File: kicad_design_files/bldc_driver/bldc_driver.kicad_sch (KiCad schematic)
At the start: 2 parts

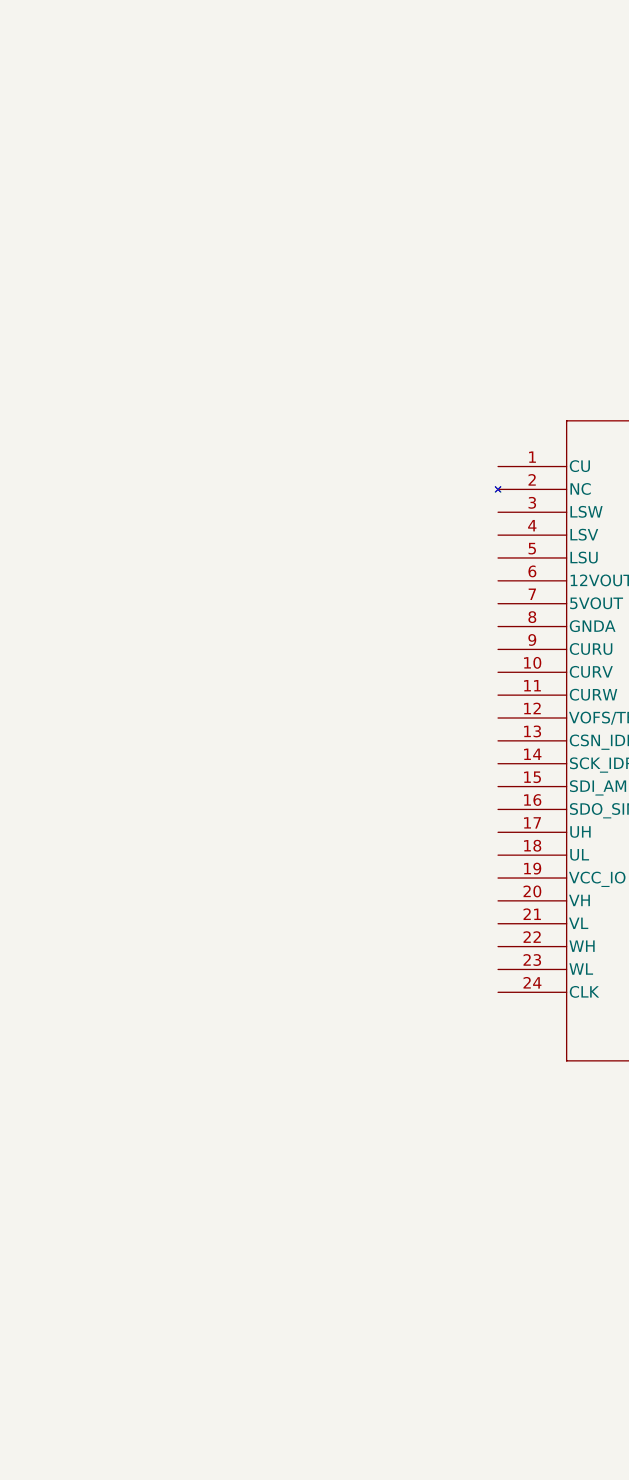
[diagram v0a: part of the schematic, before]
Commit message: MOSFET is determined
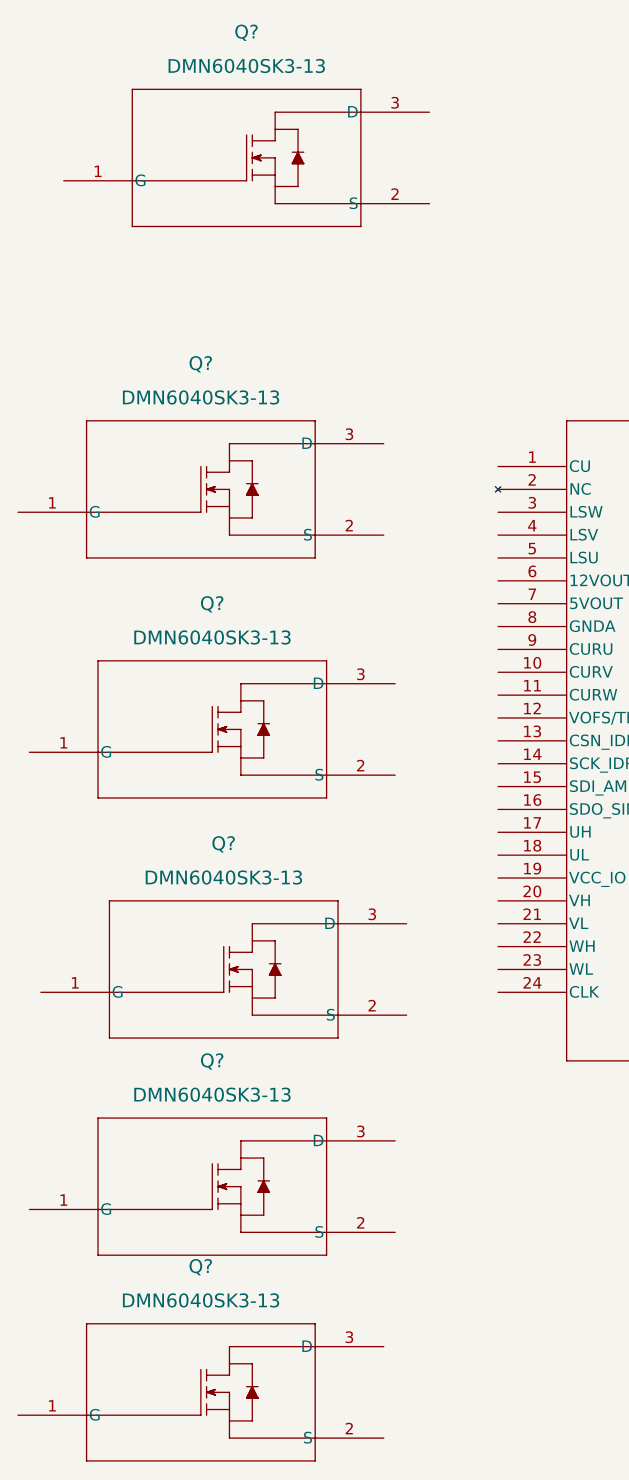
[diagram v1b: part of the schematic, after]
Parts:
- added Q? (x6): DMN6040SK3-13, bldcDriverFootprintLibrary:D-PAK_DMN6040SK3-13_DIO, symbol bldcDriverLibrary:DMN6040SK3-13
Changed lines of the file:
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@@
 (kicad_sch (version 20211123) (generator eeschema)
   (paper "A4")
+  (symbol (lib_id "bldcDriverLibrary:DMN6040SK3-13") (at 26.67 97.79 0) (unit 1)
+    (in_bom yes) (on_board yes) (fields_autoplaced)
+    (property "Reference" "Q?" (id 0) (at 46.99 81.28 0)
+      (effects (font (size 1.524 1.524)))
+    )
+    (property "Value" "DMN6040SK3-13" (id 1) (at 46.99 85.09 0)
+      (effects (font (size 1.524 1.524)))
+    )
+    (property "Footprint" "bldcDriverFootprintLibrary:D-PAK_DMN6040SK3-13_DIO" (id 2) (at 26.67 97.79 0)
+      (effects (font (size 1.27 1.27) italic) hide)
+    )
+    (property "Datasheet" "DMN6040SK3-13" (id 3) (at 26.67 97.79 0)
+      (effects (font (size 1.27 1.27) italic) hide)
+    )
+    (pin "1")
+    (pin "2")
+    (pin "3")
+  )
+  (symbol (lib_id "bldcDriverLibrary:DMN6040SK3-13") (at 27.94 124.46 0) (unit 1)
+    (in_bom yes) (on_board yes) (fields_autoplaced)
+    (property "Reference" "Q?" (id 0) (at 48.26 107.95 0)
+      (effects (font (size 1.524 1.524)))
+    )
+    (property "Value" "DMN6040SK3-13" (id 1) (at 48.26 111.76 0)
+      (effects (font (size 1.524 1.524)))
+    )
+    (property "Footprint" "bldcDriverFootprintLibrary:D-PAK_DMN6040SK3-13_DIO" (id 2) (at 27.94 124.46 0)
+      (effects (font (size 1.27 1.27) italic) hide)
+    )
+    (property "Datasheet" "DMN6040SK3-13" (id 3) (at 27.94 124.46 0)
+      (effects (font (size 1.27 1.27) italic) hide)
+    )
+    (pin "1")
+    (pin "2")
+    (pin "3")
+  )
   (symbol (lib_id "bldcDriverLibrary:TMC6200-TA-T") (at 78.74 66.04 0) (unit 1)
     (in_bom yes) (on_board yes) (fields_autoplaced)
@@
     (pin "EPAD")
   )
+  (symbol (lib_id "bldcDriverLibrary:DMN6040SK3-13") (at 25.4 71.12 0) (unit 1)
+    (in_bom yes) (on_board yes) (fields_autoplaced)
+    (property "Reference" "Q?" (id 0) (at 45.72 54.61 0)
+      (effects (font (size 1.524 1.524)))
+    )
+    (property "Value" "DMN6040SK3-13" (id 1) (at 45.72 58.42 0)
+      (effects (font (size 1.524 1.524)))
+    )
+    (property "Footprint" "bldcDriverFootprintLibrary:D-PAK_DMN6040SK3-13_DIO" (id 2) (at 25.4 71.12 0)
+      (effects (font (size 1.27 1.27) italic) hide)
+    )
+    (property "Datasheet" "DMN6040SK3-13" (id 3) (at 25.4 71.12 0)
+      (effects (font (size 1.27 1.27) italic) hide)
+    )
+    (pin "1")
+    (pin "2")
+    (pin "3")
+  )
   (symbol (lib_id "bldcDriverLibrary:ESP32-WROOM-32U") (at 234.95 91.44 0) (unit 1)
     (in_bom yes) (on_board yes) (fields_autoplaced)
@@
     (pin "9")
   )
+  (symbol (lib_id "bldcDriverLibrary:DMN6040SK3-13") (at 30.48 34.29 0) (unit 1)
+    (in_bom yes) (on_board yes) (fields_autoplaced)
+    (property "Reference" "Q?" (id 0) (at 50.8 17.78 0)
+      (effects (font (size 1.524 1.524)))
+    )
+    (property "Value" "DMN6040SK3-13" (id 1) (at 50.8 21.59 0)
+      (effects (font (size 1.524 1.524)))
+    )
+    (property "Footprint" "bldcDriverFootprintLibrary:D-PAK_DMN6040SK3-13_DIO" (id 2) (at 30.48 34.29 0)
+      (effects (font (size 1.27 1.27) italic) hide)
+    )
+    (property "Datasheet" "DMN6040SK3-13" (id 3) (at 30.48 34.29 0)
+      (effects (font (size 1.27 1.27) italic) hide)
+    )
+    (pin "1")
+    (pin "2")
+    (pin "3")
+  )
+  (symbol (lib_id "bldcDriverLibrary:DMN6040SK3-13") (at 25.4 171.45 0) (unit 1)
+    (in_bom yes) (on_board yes) (fields_autoplaced)
+    (property "Reference" "Q?" (id 0) (at 45.72 154.94 0)
+      (effects (font (size 1.524 1.524)))
+    )
+    (property "Value" "DMN6040SK3-13" (id 1) (at 45.72 158.75 0)
+      (effects (font (size 1.524 1.524)))
+    )
+    (property "Footprint" "bldcDriverFootprintLibrary:D-PAK_DMN6040SK3-13_DIO" (id 2) (at 25.4 171.45 0)
+      (effects (font (size 1.27 1.27) italic) hide)
+    )
+    (property "Datasheet" "DMN6040SK3-13" (id 3) (at 25.4 171.45 0)
+      (effects (font (size 1.27 1.27) italic) hide)
+    )
+    (pin "1")
+    (pin "2")
+    (pin "3")
+  )
+  (symbol (lib_id "bldcDriverLibrary:DMN6040SK3-13") (at 26.67 148.59 0) (unit 1)
+    (in_bom yes) (on_board yes) (fields_autoplaced)
+    (property "Reference" "Q?" (id 0) (at 46.99 132.08 0)
+      (effects (font (size 1.524 1.524)))
+    )
+    (property "Value" "DMN6040SK3-13" (id 1) (at 46.99 135.89 0)
+      (effects (font (size 1.524 1.524)))
+    )
+    (property "Footprint" "bldcDriverFootprintLibrary:D-PAK_DMN6040SK3-13_DIO" (id 2) (at 26.67 148.59 0)
+      (effects (font (size 1.27 1.27) italic) hide)
+    )
+    (property "Datasheet" "DMN6040SK3-13" (id 3) (at 26.67 148.59 0)
+      (effects (font (size 1.27 1.27) italic) hide)
+    )
+    (pin "1")
+    (pin "2")
+    (pin "3")
+  )
   (sheet_instances
     (path "/" (page "1"))
   )
   (symbol_instances
+    (path "/0528159b-171b-4814-8fbd-424a49af9ff9"
+      (reference "Q?") (unit 1) (value "DMN6040SK3-13") (footprint "bldcDriverFootprintLibrary:D-PAK_DMN6040SK3-13_DIO")
+    )
+    (path "/5f76af1d-e25d-4b55-ba28-8df48b44feb7"
+      (reference "Q?") (unit 1) (value "DMN6040SK3-13") (footprint "bldcDriverFootprintLibrary:D-PAK_DMN6040SK3-13_DIO")
+    )
+    (path "/7ecf728e-7e84-4b67-a832-16cb58f85177"
+      (reference "Q?") (unit 1) (value "DMN6040SK3-13") (footprint "bldcDriverFootprintLibrary:D-PAK_DMN6040SK3-13_DIO")
+    )
+    (path "/9280bad1-e9ff-40cf-bdde-8958bd6789b3"
+      (reference "Q?") (unit 1) (value "DMN6040SK3-13") (footprint "bldcDriverFootprintLibrary:D-PAK_DMN6040SK3-13_DIO")
+    )
+    (path "/a3c012d8-5b76-42c7-9b98-0158f83581ad"
+      (reference "Q?") (unit 1) (value "DMN6040SK3-13") (footprint "bldcDriverFootprintLibrary:D-PAK_DMN6040SK3-13_DIO")
+    )
+    (path "/a3ce6787-f633-4143-b22e-68797e7b10bf"
+      (reference "Q?") (unit 1) (value "DMN6040SK3-13") (footprint "bldcDriverFootprintLibrary:D-PAK_DMN6040SK3-13_DIO")
+    )
     (path "/61391d01-5eeb-4a2b-9139-3891e5eb64ee"
       (reference "U?") (unit 1) (value "TMC6200-TA-T") (footprint "bldcDriverFootprintLibrary:eTQFP48_9x9_TRI")

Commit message: Schematic Design Completed
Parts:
- removed U?: TMC6200-TA-T, bldcDriverFootprintLibrary:eTQFP48_9x9_TRI, symbol bldcDriverLibrary:TMC6200-TA-T
- removed U?: ESP32-WROOM-32U, bldcDriverFootprintLibrary:XCVR_ESP32-WROOM-32U, symbol bldcDriverLibrary:ESP32-WROOM-32U
- added C1: 22uF_10V_X5R_±20%_0805, bldcDriverFootprintLibrary:C_0805_2012Metric_Pad1.18x1.45mm_HandSolder, symbol bldcDriverLibrary:22uF_10V_X5R_±20%_0805
- added C2: 10uF_25V_0805, bldcDriverFootprintLibrary:C_0805_2012Metric_Pad1.18x1.45mm_HandSolder, symbol bldcDriverLibrary:10uF_25V_X5R_±10%_0805
- added H1, H2, H3, H4: MountingHole, MountingHole:MountingHole_3.2mm_M3, symbol Mechanical:MountingHole
- added J1: TBP01R1-508-02BE, bldcDriverFootprintLibrary:CUI_TBP01R1-508-02BE, symbol bldcDriverLibrary:TBP01R1-508-02BE
- added J2: TBP01R1-508-03BE, bldcDriverFootprintLibrary:CUI_TBP01R1-508-03BE, symbol bldcDriverLibrary:TBP01R1-508-03BE
- added J3: 530480210, bldcDriverFootprintLibrary:CON_530480210_MOL, symbol bldcDriverLibrary:530480210
- added J4: 530480510, bldcDriverFootprintLibrary:CON_530480510_MOL, symbol bldcDriverLibrary:530480510
- added LED1: B1911PG--20D000514U1930, bldcDriverFootprintLibrary:LED_B1911PG--20D000514U1930_HVK, symbol bldcDriverLibrary:B1911PG--20D000514U1930
- added R1: 4.7kΩ_±20%_1/4W_0402, bldcDriverFootprintLibrary:R_0402_1005Metric_Pad0.72x0.64mm_HandSolder, symbol bldcDriverLibrary:4.7kΩ_±20%_1/4W_0402
- added R2, R3: 10kΩ_±20%_1/4W_0402, bldcDriverFootprintLibrary:R_0402_1005Metric_Pad0.72x0.64mm_HandSolder, symbol bldcDriverLibrary:10kΩ_±20%_1/4W_0402
- added R4, R5, R6: 10mΩ_2512, Resistor_SMD:R_2512_6332Metric, symbol bldcDriverLibrary:10mΩ_±1%_5W_2512
- added U1: AZ1117ID-3.3TRG1, bldcDriverFootprintLibrary:TO252-2_AZ1117ID-3.3TRG1_DIO, symbol bldcDriverLibrary:AZ1117ID-3.3TRG1
- gave numbers to parts that had none: 6
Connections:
- net HW: now reaches Q3.1 (G)
- net W: now reaches Q3.2 (S)
- net W: now also Q6.3 (D), R4.1
- net VIN: now reaches Q3.3 (D)
- net VIN: now also Q1.3 (D), Q2.3 (D), J1.1
- net LV: now reaches Q5.1 (G)
- net GND: now reaches Q5.2 (S)
- net GND: now also Q4.2 (S), Q6.2 (S), C1.2, C2.1, J1.2, J4.5, R1.2, U1.1 (ADJ/GND)
- net V: now reaches Q5.3 (D)
- net V: now also Q2.2 (S), R5.2
- net HU: now reaches Q1.1 (G)
- net U: now reaches Q1.2 (S)
- net U: now also Q4.3 (D), R6.1
- net LW: now reaches Q6.1 (G)
- net LU: now reaches Q4.1 (G)
- net HV: now reaches Q2.1 (G)
- new net: LED1.1, R1.1
- new net +12V: C2.2, U1.3 (INPUT)
- new net +3.3V: C1.1, J4.1, LED1.2, R2.2, R3.2, U1.2 (OUTPUT)
- new net HALL_U: J4.2
- new net HALL_V: J4.3
- new net HALL_W: J4.4
- new net I2CSCL: J3.1, R2.1
- new net I2CSDA: J3.2, R3.1
- new net PHASEU: J2.1, R6.2
- new net PHASEV: J2.2
- new net PHASEW: J2.3, R4.2
- new net PHASE_V: R5.1
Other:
- added sheet esp32 (esp32.kicad_sch)
- added sheet gateDriver (gateDriver.kicad_sch)
- note added: "LEDs: Green : 3.3V is active & DRV_EN is high Blue : Programming Mode is active Red : FAULT is high"
- moved on the sheet: Q1, Q2, Q3, Q4, Q5, Q6

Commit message: Done
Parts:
- removed H1, H2, H3, H4: MountingHole, MountingHole:MountingHole_3.2mm_M3, symbol Mechanical:MountingHole
- added H1, H2, H3, H4: MountingHole_Pad, MountingHole:MountingHole_3.2mm_M3_DIN965_Pad, symbol Mechanical:MountingHole_Pad
- renumbered Q4 to Q2, Q2 to Q3, Q5 to Q4, Q3 to Q5
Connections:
- net PHASEV is gone; now on net PHASE_V: J2.2
- net GND: now also H1.1, H2.1, H3.1, H4.1
- net PHASEU renamed PHASE_U
- net PHASEW renamed PHASE_W
